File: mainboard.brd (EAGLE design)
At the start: 90.2 x 95.9 mm, 70 parts, among them T1 SINGLE_NCHAN_FET, T2 MOSFET_PCHAN_20A, T3 SINGLE_NCHAN_FET, T4 MOSFET_PCHAN_20A, T5 SINGLE_NCHAN_FET, T6 MOSFET_PCHAN_20A, U1 MURATA_REG_OKL-T3-W12, U2 TEENSY_3.0+4, U3 RFM23BP, U4 HMC5883LSMD, U5 ITG-3200, U6 AB0805, U7 CURRENT_MAX4372, U8 CURRENT_MAX4372, X1 CRYSTAL.ABS07

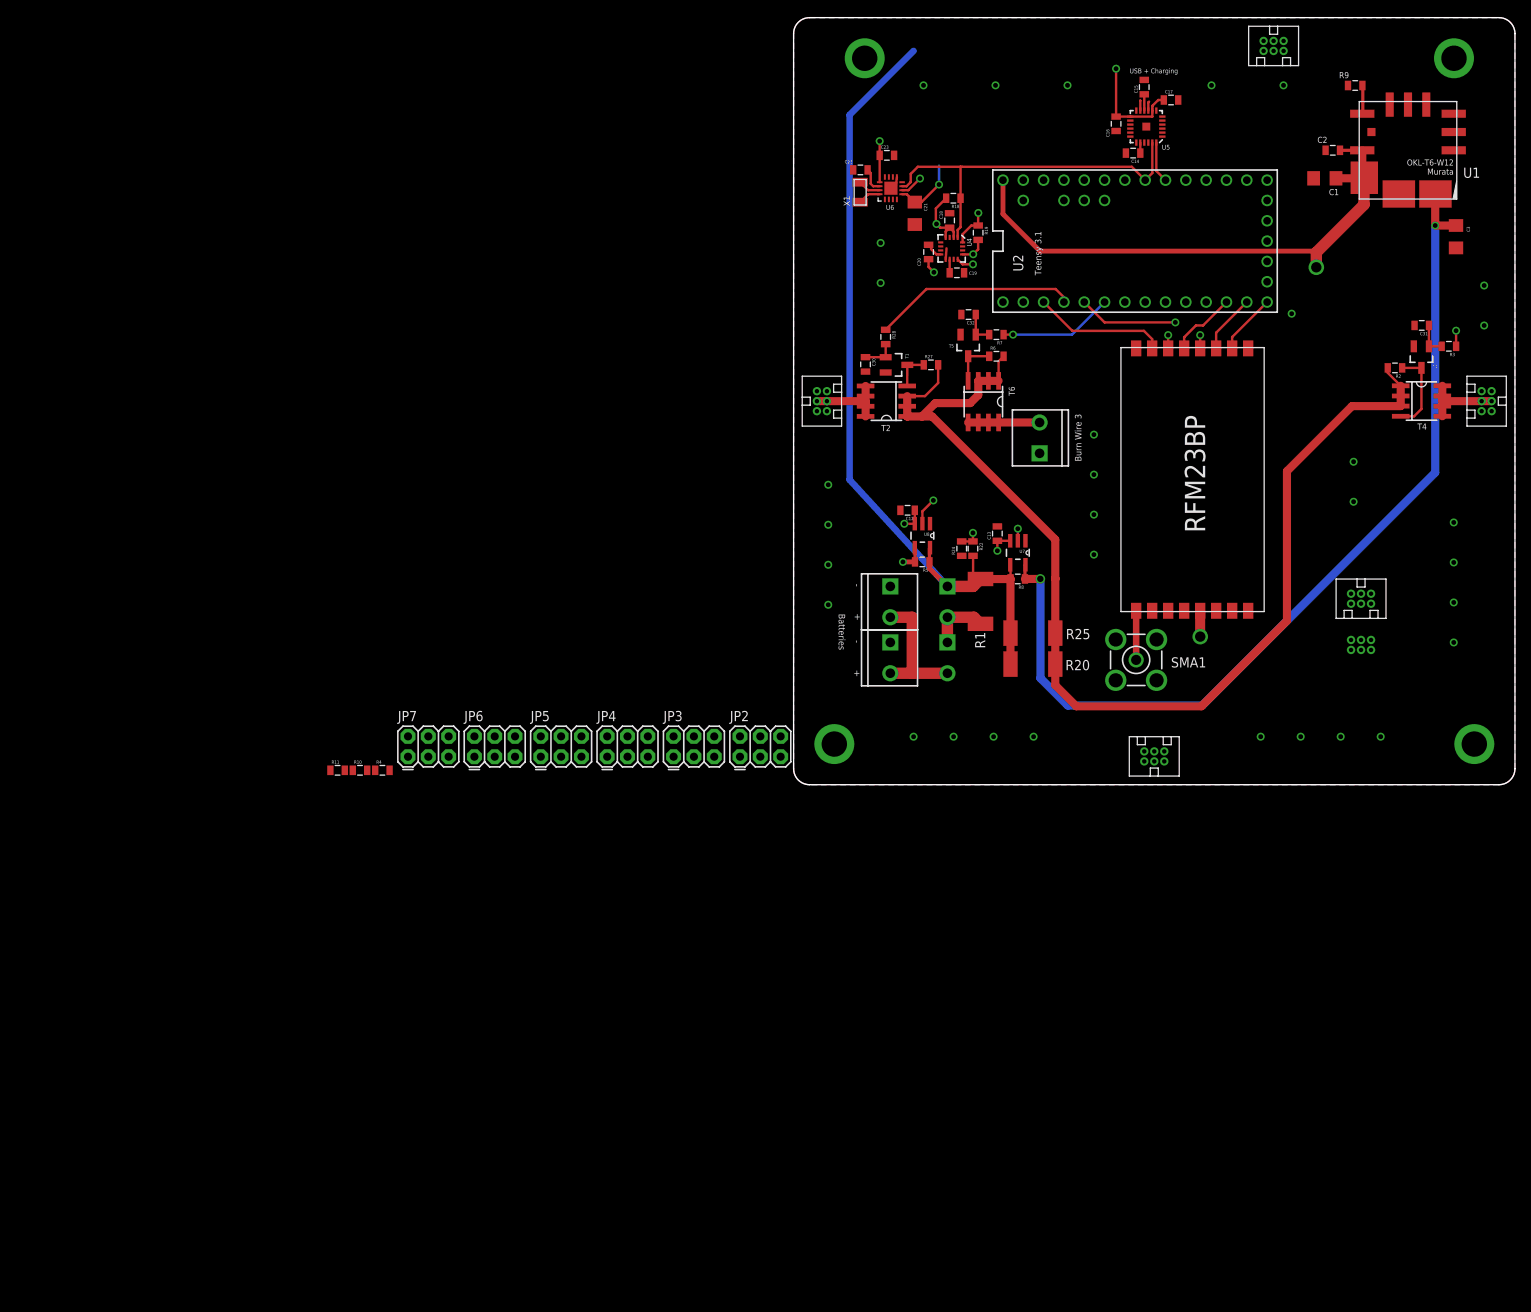
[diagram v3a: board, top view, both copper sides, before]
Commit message: Added stuff to mainboard for NanoRacks requirements
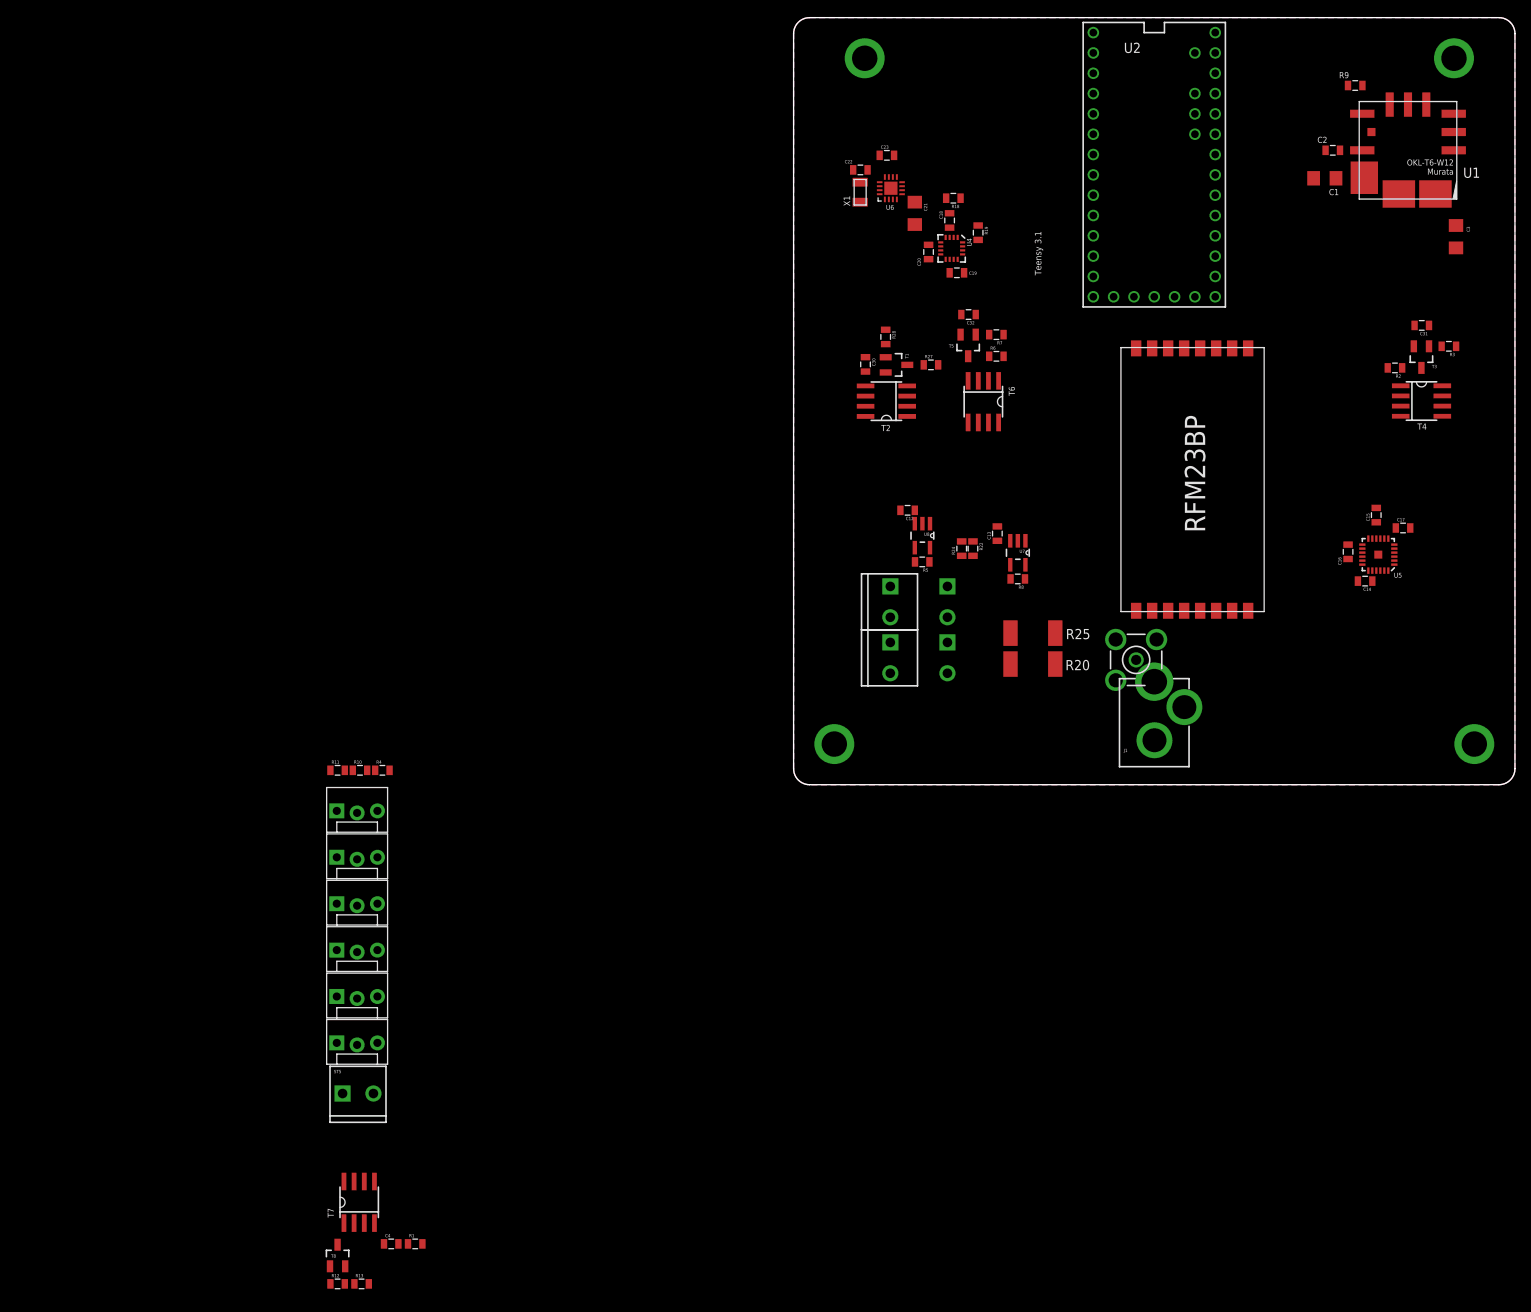
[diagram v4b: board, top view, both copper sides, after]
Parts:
- removed G1, G2, G3, G4, G5, G6: G125-FV20605L0P, G125-FV20605L0P:G125-FV20605L0P
- removed JP2, JP3, JP4, JP5, JP6, JP7: (no value), SparkFun-Connectors:2X3
- added C4: .1uF, SparkFun-Capacitors:0805
- added J1: POWER_JACKPTH_LOCK, SparkFun-Connectors:POWER_JACK_PTH_LOCK
- added JP1, JP10, JP11, JP12, JP8, JP9: (no value), SparkFun-Connectors:MOLEX-1X3_LOCK
- added R12: 10K, SparkFun-Resistors:0805
- added R13: 4.7K, SparkFun-Resistors:0805
- added T7: MOSFET_PCHAN_20A, phonesat:SO8
- added T8: SINGLE_NCHAN_FET, phonesat:SOT23-3
- R1: value 0R -> 3K3; device SparkFun-Resistors:R2512 -> SparkFun-Resistors:0805
- moved ST5 118.3 mm to (-56.2, -38.6), turned to 0 degrees
- moved R1 107.0 mm to (-47.3, -57.4), turned to 0 degrees
- moved C17 60.9 mm to (76.2, 32.1)
- moved C14 60.9 mm to (71.4, 25.4)
- moved C15 60.9 mm to (72.8, 33.7)
- moved C16 60.9 mm to (69.3, 29.1)
- moved U5 60.9 mm to (73.1, 28.8)
- moved U2 9.85 mm to (45.1, 77.5), turned to 0 degrees
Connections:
- new net ENAB_BURN4: R12.1, R13.2
- new net N$1: ST1.2, ST2.2, ST5.1
- new net N$8: C4.1, R12.2, T8.1
- new net N$9: R1.1, T7.4, T8.3
- new net VBURN4: T7.5, T7.6, T7.7, T7.8
- net BATT_INPUT: now also J1.PWR, ST1.1, ST2.1; no longer ST1.2, ST2.2
- net GND: now also C4.2, J1.GND, J1.GNDBREAK, JP1.1, JP10.1, JP11.1, JP12.1, JP8.1, JP9.1, R13.1, ST5.2, T8.2; no longer G1.P1, G1.P4, G2.P1, G2.P4, G3.P1, G3.P4, G4.P1, G4.P4, G5.P1, G5.P4, G6.P1, G6.P4, JP2.2, JP3.2, JP4.2, JP5.2, JP6.2, JP7.2, ST1.1, ST2.1, ST5.1
- net N$4: no longer R1.1
- net VBATT: no longer R1.2
- net VBURN1: now also JP1.3; no longer G4.P2, G4.P5
- net VBURN2: now also JP8.3; no longer G2.P2, G2.P5
- net VBURN3: now also JP9.3; no longer ST5.2
- net VBURN_IN: now also R1.2, T7.1, T7.2, T7.3
- net VSOLAR: now also JP1.2, JP10.2, JP11.2, JP12.2, JP8.2, JP9.2; no longer G1.P3, G1.P6, G2.P3, G2.P6, G3.P3, G3.P6, G4.P3, G4.P6, G5.P3, G5.P6, G6.P3, G6.P6
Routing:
- net VBURN_IN: track 144.5 -> 0.00 mm
- net 5V: track 128.5 -> 0.00 mm, vias 2 -> 0
- net VREG_IN: track 116.4 -> 0.00 mm, vias 2 -> 0
- net VBATT: track 105.3 -> 0.00 mm
- net N$37: track 59.7 -> 0.00 mm, vias 1 -> 0
- net I_SOLAR: track 57.6 -> 0.00 mm, vias 1 -> 0
- net I_BATT: track 56.9 -> 0.00 mm, vias 1 -> 0
- net ENAB_BURN2: track 50.8 -> 0.00 mm, vias 3 -> 0
- net I2C_SDA: track 47.2 -> 0.00 mm, vias 2 -> 0
- net I2C_SCL: track 46.7 -> 0.00 mm
- net 3.3V: track 44.9 -> 0.00 mm, vias 7 -> 0
- net ENAB_BURN1: track 25.4 -> 0.00 mm
- net SPI_SCK: track 24.5 -> 0.00 mm, vias 1 -> 0
- net RF_NIRQ: track 21.5 -> 0.00 mm, vias 1 -> 0
- net BATT_INPUT: track 16.9 -> 0.00 mm
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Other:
- board text removed: "+"
- board text removed: "-"
- board text removed: "Batteries"
- board text removed: "Burn Wire 3"
- board text removed: "USB + Charging"

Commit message: Adding Arduino Pro Mini to Mainboard
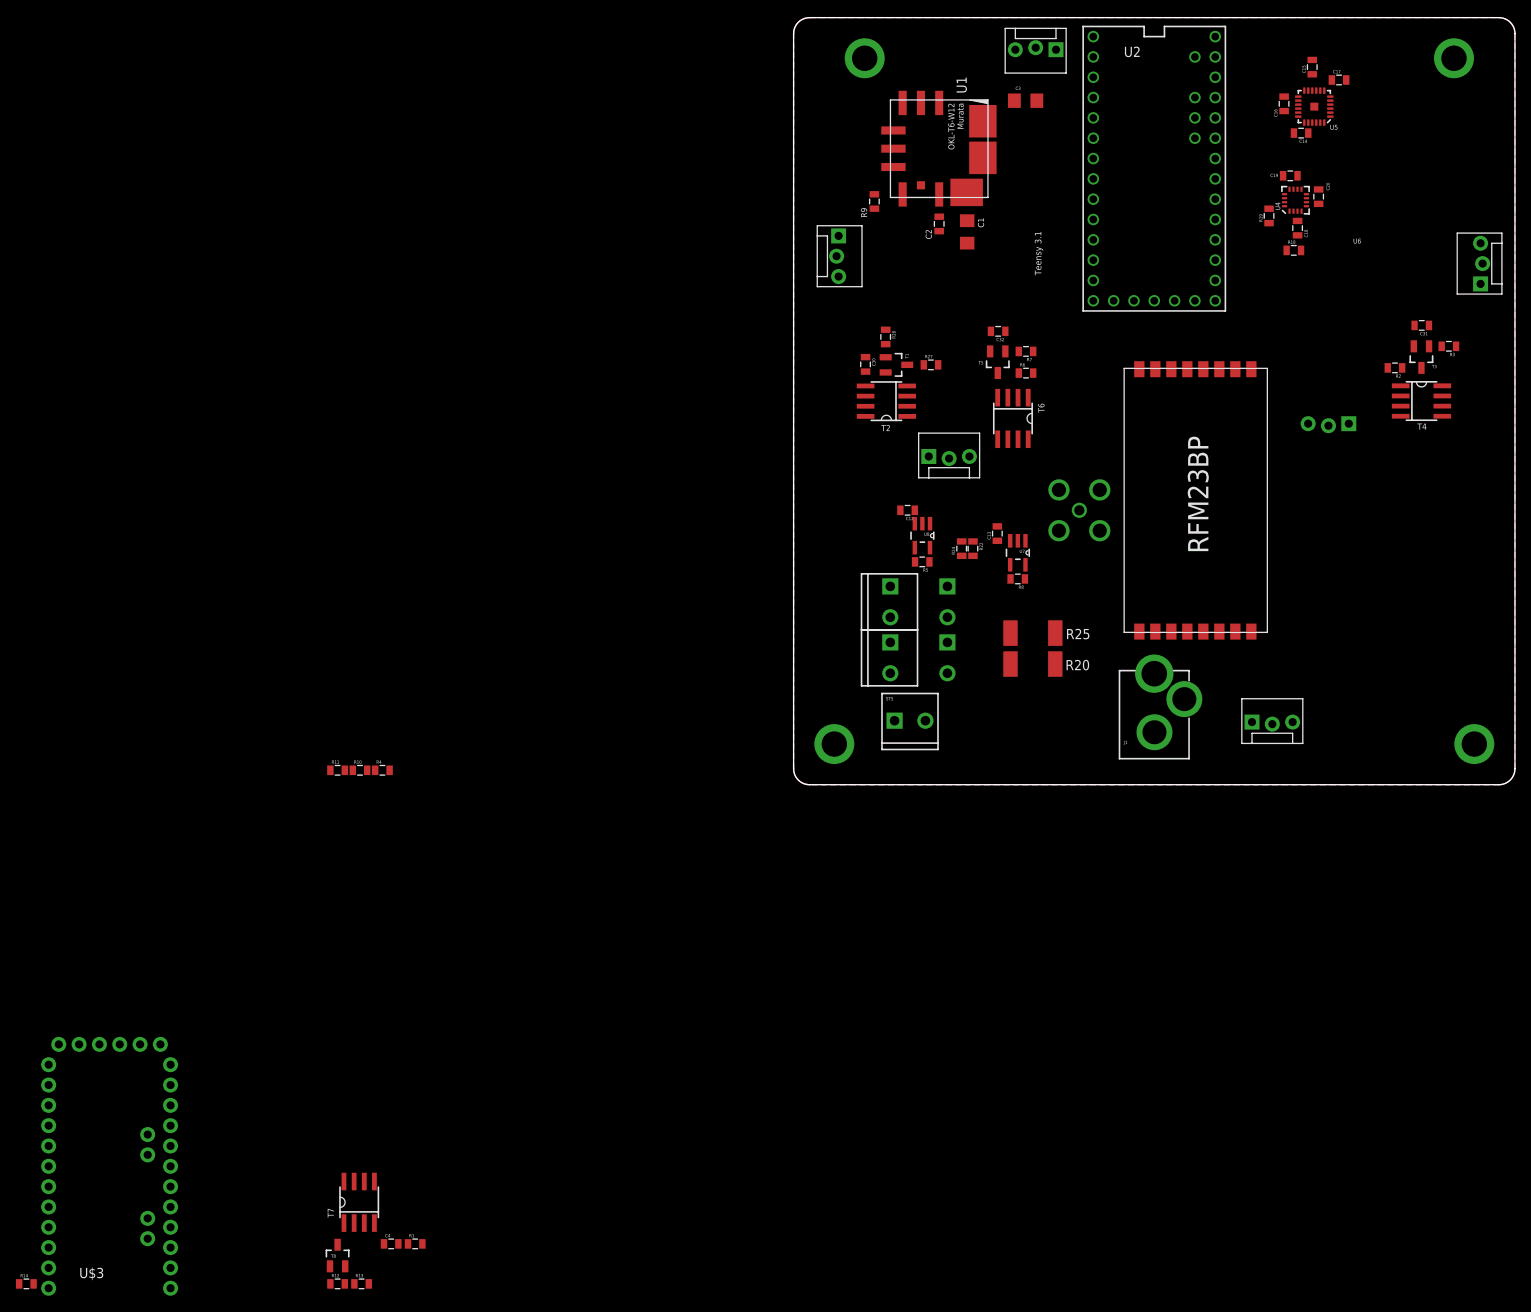
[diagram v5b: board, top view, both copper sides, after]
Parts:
- removed C21: 100uF, SparkFun-Capacitors:1206
- removed C22: 47pF, SparkFun-Capacitors:0805
- removed C23: 0.1uF, SparkFun-Capacitors:0805
- removed U6: AB0805, AB0805:QFN16
- removed X1: CRYSTAL.ABS07, abracon:ABS07
- added R14: 10k, SparkFun-Resistors:0805
- added U$3: ARDUINO_PRO_MINI, SparkFun-Boards:ARDUINO_PRO_MINI
- moved JP8 160.1 mm to (86.0, 62.6), turned to 90 degrees
- moved JP12 153.5 mm to (32.8, 92.0), turned to 180 degrees
- moved JP10 142.6 mm to (69.4, 45.0), flipped to the bottom
- moved JP11 119.4 mm to (57.3, 7.70)
- moved JP1 95.4 mm to (5.50, 68.6), turned to 270 degrees
- moved JP9 92.7 mm to (16.9, 40.9)
- moved ST5 83.3 mm to (12.8, 8.00)
- moved R9 61.8 mm to (10.1, 72.9), turned to 270 degrees
- moved U1 58.6 mm to (18.2, 79.5), turned to 270 degrees
- moved C14 56.6 mm to (63.4, 81.5)
- moved C15 56.6 mm to (64.8, 89.7)
- moved C16 56.6 mm to (61.3, 85.1)
- moved C17 56.6 mm to (68.2, 88.1)
- moved U5 56.6 mm to (65.1, 84.8)
- moved C3 56.4 mm to (29.0, 85.5), turned to 0 degrees
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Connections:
- net UART_RX renamed UART3_RX
- net UART_TX renamed UART3_TX
- removed net N$38: U6.XI, X1.1
- removed net N$41: U6.XO, X1.2
- removed net N$45: C22.1, U6.AF
- new net N$10: R14.2, U$3.10
- new net N_ENAB_REG: U1.1
- new net UART1_RX: U$3.1, U2.0
- new net UART1_TX: U$3.2, U2.1
- net 3.3V: no longer C21.1, C23.1, U6.VBAT, U6.VCC
- net ENAB_BURN1: now also U2.3; no longer U2.2
- net ENAB_BURN2: now also U2.4; no longer U2.3
- net ENAB_BURN3: now also U2.5; no longer U2.4
- net ENAB_BURN4: now also U2.6
- net GND: now also R14.1, U$3.23, U$3.4; no longer C21.2, C22.2, C23.2, U1.1, U6.GND, U6.GNDPAD
- net I2C_SCL: no longer U6.SCL
- net I2C_SDA: no longer U6.SDA
- net RF_NIRQ: now also U2.2; no longer U2.0
- net RF_SDN: now also U2.9; no longer U2.1
- net VBATT: now also U$3.24
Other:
- board text added: "Main Board V1.2"
- board text removed: "Main Board V1.0"

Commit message: Added switches for programming mode
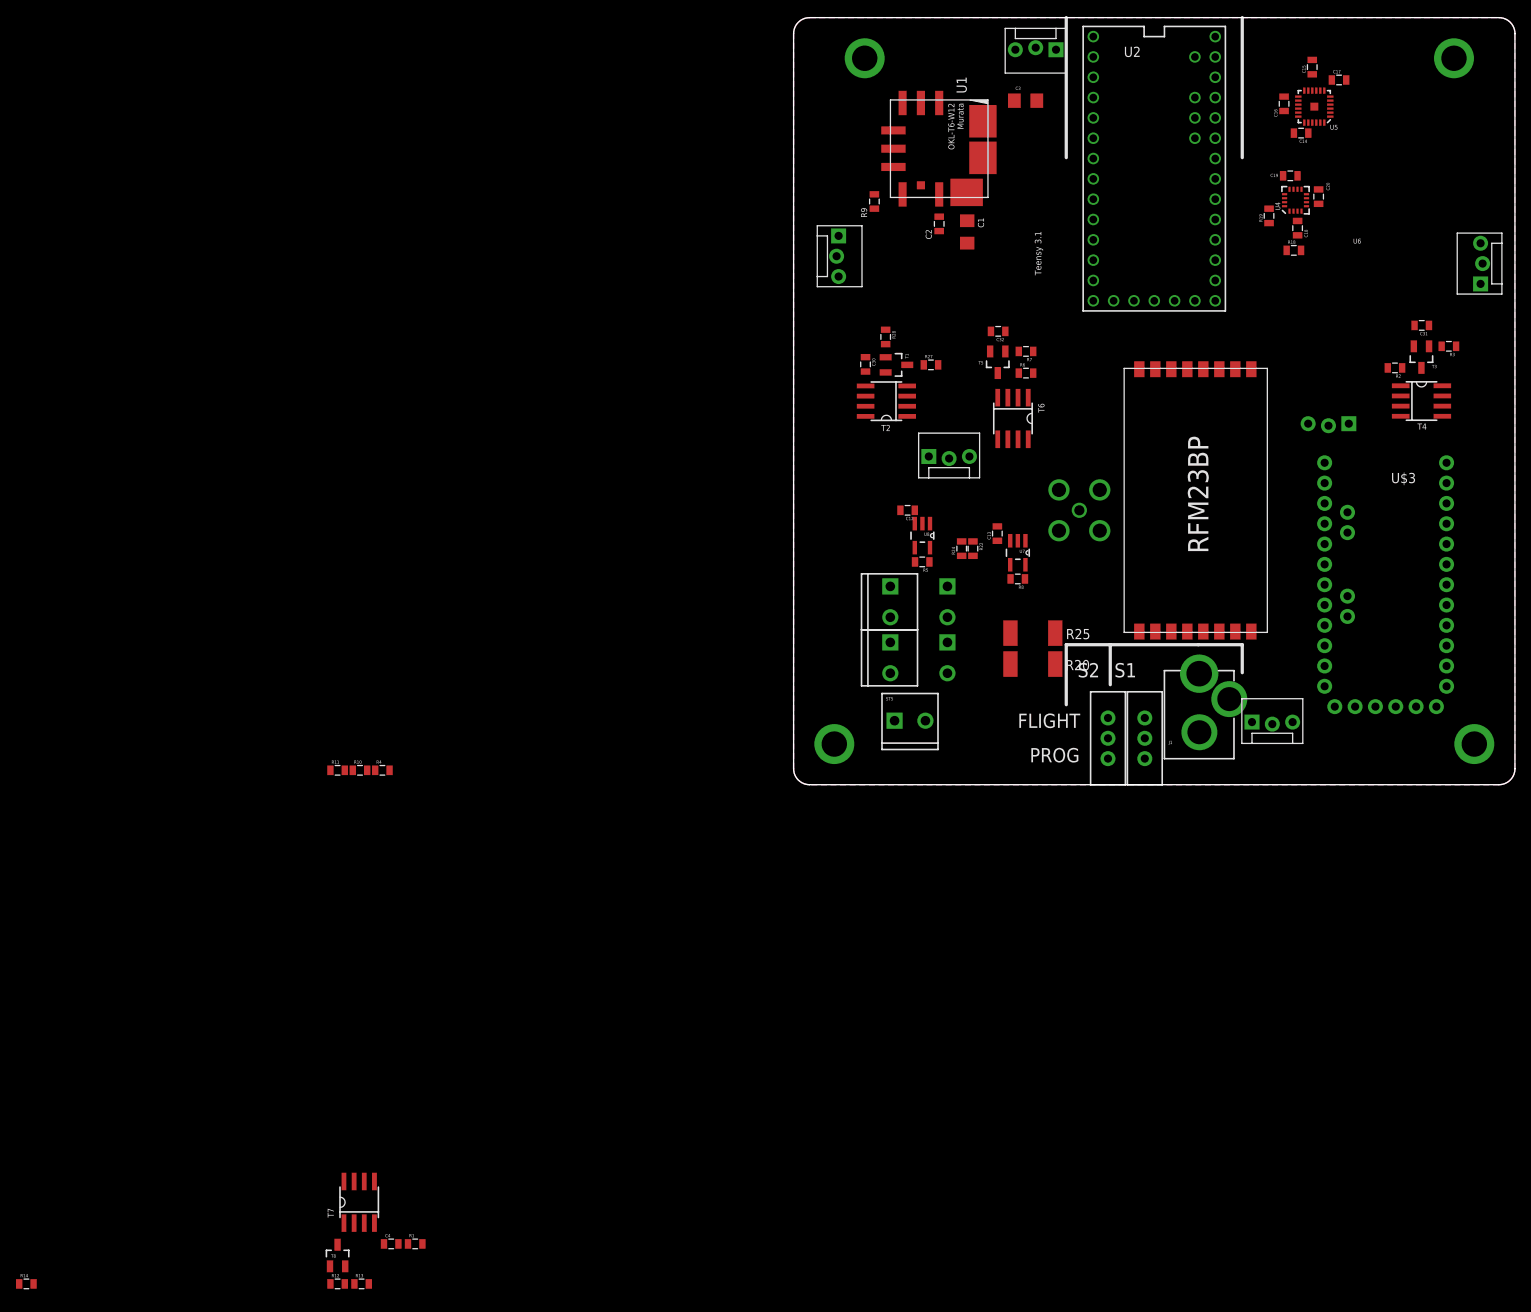
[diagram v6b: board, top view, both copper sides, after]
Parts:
- added S1, S2: (no value), SparkFun-Electromechanical:SWITCH-SPDT
- moved U$3 175.3 mm to (74.0, 25.0), turned to 180 degrees
- moved J1 5.62 mm to (50.7, 0.00)
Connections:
- removed net N$10: R14.2, U$3.10
- removed net VUSB: U2.VUSB
- new net N$11: S1.2, U2.23/A9
- new net N$13: S2.2, U2.VUSB
- new net PGM_RST: S1.3, U$3.22
- new net PGM_VCC: S2.3, U$3.21
- net N_ENAB_REG: now also R14.2, U$3.10
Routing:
- added copper zone on layer 1, net 5V
- removed copper zone on layer 1, net GND
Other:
- board text added: "FLIGHT"
- board text added: "PROG"
